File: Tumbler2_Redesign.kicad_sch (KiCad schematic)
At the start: 4 parts

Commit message: Sketch out component placement
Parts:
- H1, H2, H3, H4: footprint MountingHole:MountingHole_3mm_Pad -> MountingHole:MountingHole_3mm_Pad_Via
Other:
- sheet MCU ports: added INT1; removed INT
- sheet Peripherals ports: added INT1; removed INT

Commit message: Fix bus merging and add net classes
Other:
- sheet MCU ports: added {MOT_A}, {MOT_B}; removed {MOT1}, {MOT2}
- sheet Peripherals ports: added {MOT_A}, {MOT_B}; removed {MOT1}, {MOT2}
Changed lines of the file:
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@@
 	)
 	(bus_alias "USB1"
-		(members "DP" "DM")
+		(members "DP_1" "DN_1")
 	)
 	(bus_alias "USB2"
-		(members "DP" "DM")
+		(members "DP_2" "DN_2")
 	)
 	(circle
@@
 			)
 		)
-		(pin "{MOT1}" bidirectional
-			(at 198.12 102.87 0)
-			(effects
-				(font
-					(size 1.27 1.27)
-				)
-				(justify right)
-			)
-		)
-		(pin "{MOT2}" bidirectional
-			(at 198.12 106.68 0)
-			(effects
-				(font
-					(size 1.27 1.27)
-				)
-				(justify right)
-			)
-		)
 		(pin "RGB" output
 			(at 198.12 121.92 0)
@@
 		(pin "INT1" input
 			(at 198.12 90.17 0)
+			(effects
+				(font
+					(size 1.27 1.27)
+				)
+				(justify right)
+			)
+		)
+		(pin "{MOT_A}" bidirectional
+			(at 198.12 102.87 0)
+			(effects
+				(font
+					(size 1.27 1.27)
+				)
+				(justify right)
+			)
+		)
+		(pin "{MOT_B}" bidirectional
+			(at 198.12 106.68 0)
 			(effects
 				(font
@@
 			)
 		)
-		(pin "{MOT1}" input
-			(at 210.82 102.87 180)
-			(effects
-				(font
-					(size 1.27 1.27)
-				)
-				(justify left)
-			)
-		)
-		(pin "{MOT2}" input
-			(at 210.82 106.68 180)
-			(effects
-				(font
-					(size 1.27 1.27)
-				)
-				(justify left)
-			)
-		)
 		(pin "INT1" output
 			(at 210.82 90.17 180)
 			(effects
 				(font
+					(size 1.27 1.27)
+				)
+				(justify left)
+			)
+		)
+		(pin "{MOT_A}" input
+			(at 210.82 102.87 180)
+			(effects
+				(font
+					(size 1.27 1.27)
+				)
+				(justify left)
+			)
+		)
+		(pin "{MOT_B}" input
+			(at 210.82 106.68 180)
+			(effects
+				(font

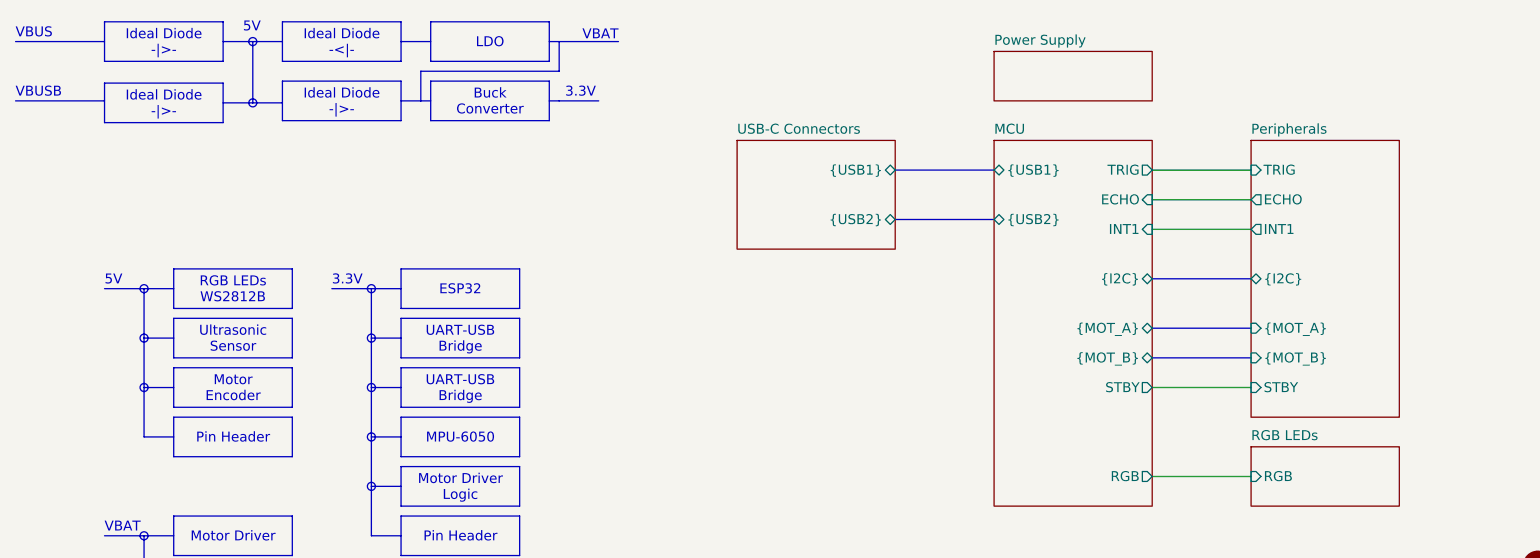
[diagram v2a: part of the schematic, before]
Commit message: Continue layout and update schematic
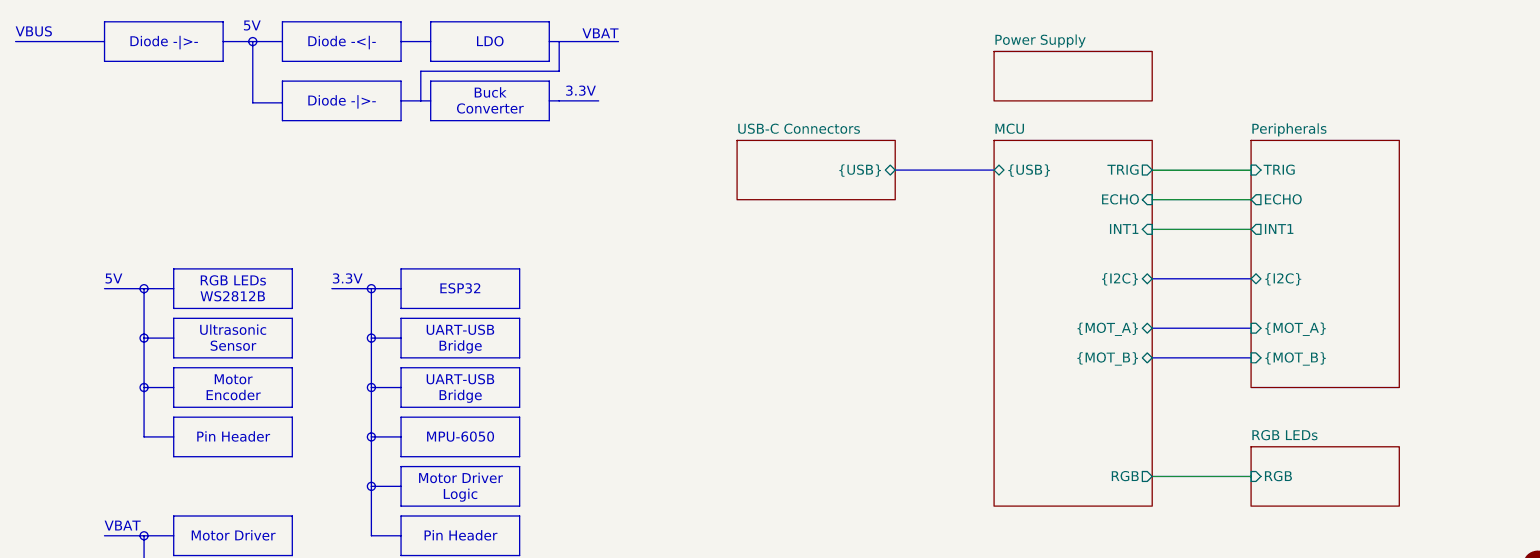
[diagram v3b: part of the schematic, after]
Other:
- sheet MCU ports: added {USB}; removed STBY, {USB1}, {USB2}
- sheet Peripherals ports: added none; removed STBY
- sheet USB-C Connectors ports: added {USB}; removed {USB1}, {USB2}
- note removed: "VBUSB"

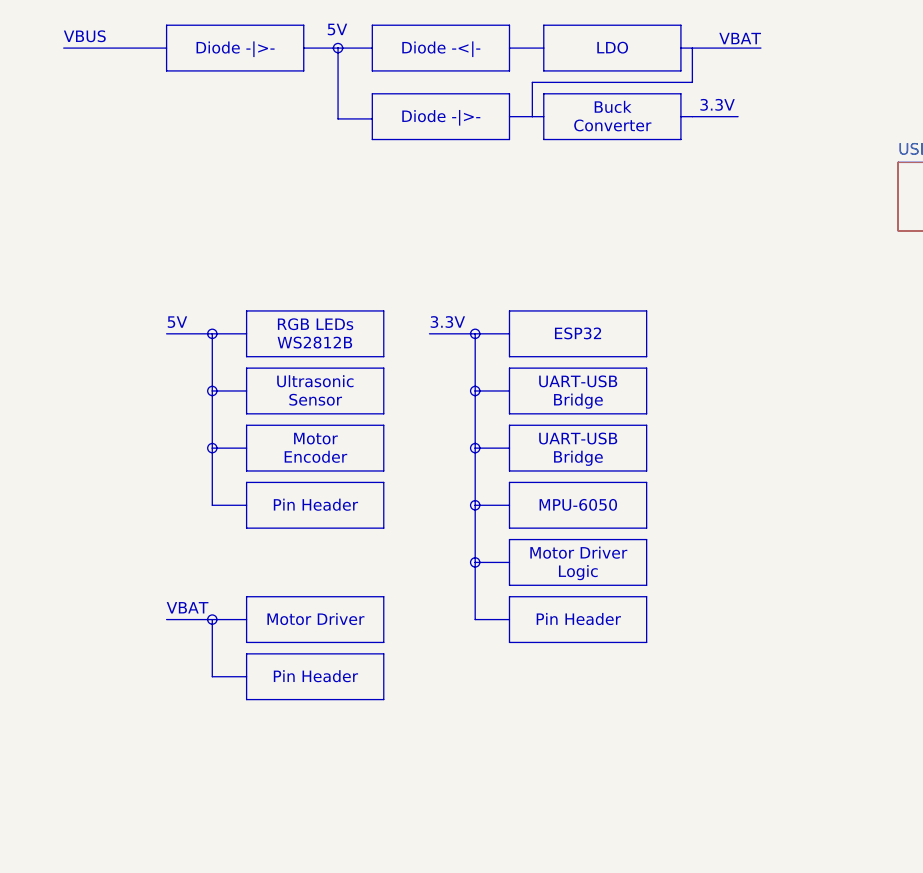
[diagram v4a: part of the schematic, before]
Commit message: Document strapping pins
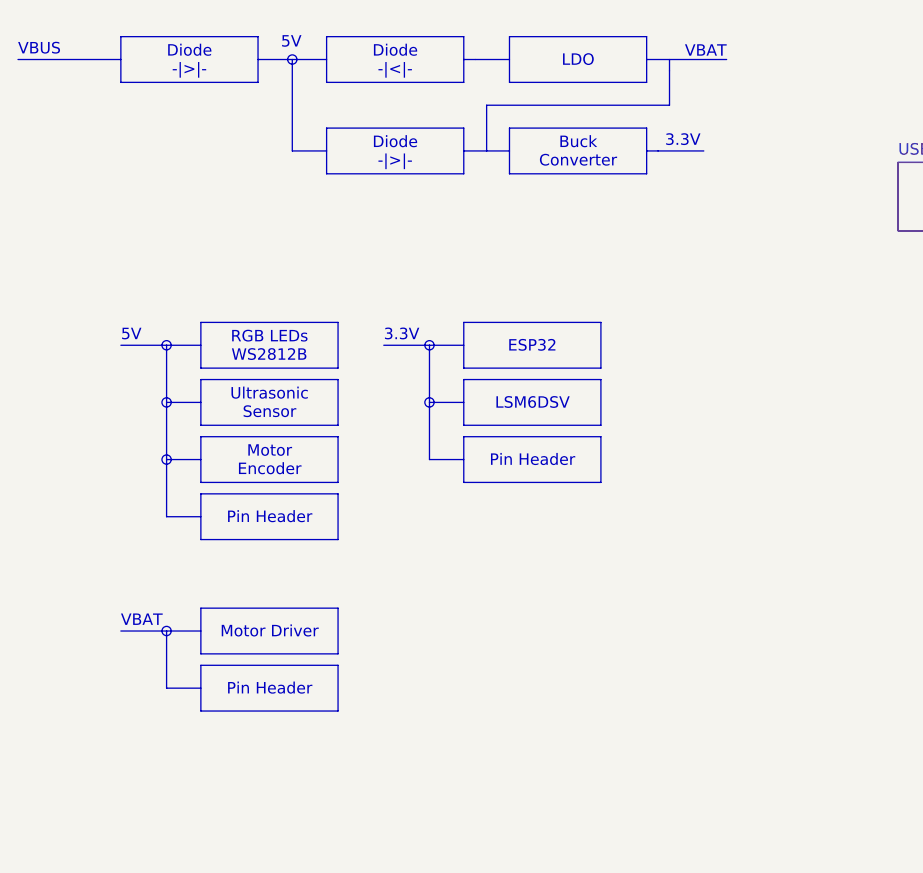
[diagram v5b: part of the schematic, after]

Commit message: Add todo list and update block diagram
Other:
- note added: "TODO: Verify output voltage levels for HC-SR04 (ECHO pin) and motor encoder Confirm whether logic HIGH is 5V, 3.3V, or lower (~2V possible) Check whether 5V or 3.3V HC-SR04 variant is used in current robots Measure actual PCB mounting hole positions Verify pin header pinout for line sensor PCB (B2B module)"
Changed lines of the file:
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@@
-	)
-	(circle
-		(center 63.5 130.81)
-		(radius 0.5142)
-		(stroke
-			(width 0)
-			(type solid)
-		)
-		(fill
-			(type color)
-			(color 0 0 194 1)
-		)
 	)
 	(circle
@@
 		)
 	)
+	(text "TODO:\nVerify output voltage levels for HC-SR04 (ECHO pin) and motor encoder\n	Confirm whether logic HIGH is 5V, 3.3V, or lower (~2V possible)\nCheck whether 5V or 3.3V HC-SR04 variant is used in current robots\nMeasure actual PCB mounting hole positions\nVerify pin header pinout for line sensor PCB (B2B module)"
+		(exclude_from_sim no)
+		(at 23.368 28.956 0)
+		(effects
+			(font
+				(size 1.27 1.27)
+			)
+			(justify left)
+		)
+	)
 	(text "VBUS"
 		(exclude_from_sim no)
@@
 	(text "VBAT"
 		(exclude_from_sim no)
-		(at 58.42 129.794 0)
+		(at 58.42 127.254 0)
 		(effects
 			(font
@@
 		)
 	)
-	(text_box "Pin Header\n"
-		(exclude_from_sim no)
-		(at 67.31 134.62 0)
-		(size 15.24 5.08)
-		(margins 0.9525 0.9525 0.9525 0.9525)
-		(stroke
-			(width 0)
-			(type solid)
-		)
-		(fill
-			(type none)
-		)
-		(effects
-			(font
-				(size 1.27 1.27)
-			)
-		)
-	)
 	(text_box "Motor Driver"
 		(exclude_from_sim no)
-		(at 67.31 128.27 0)
+		(at 67.31 125.73 0)
 		(size 15.24 5.08)
 		(margins 0.9525 0.9525 0.9525 0.9525)
@@
 	(polyline
 		(pts
-			(xy 63.5 137.16) (xy 67.31 137.16)
-		)
-		(stroke
-			(width 0)
-			(type default)
-		)
-	)
-	(polyline
-		(pts
 			(xy 63.5 105.41) (xy 67.31 105.41)
 		)
@@
 	(polyline
 		(pts
-			(xy 63.5 130.81) (xy 63.5 137.16)
-		)
-		(stroke
-			(width 0)
-			(type default)
-		)
-	)
-	(polyline
-		(pts
 			(xy 46.99 67.31) (xy 58.42 67.31)
 		)
@@
 	(polyline
 		(pts
-			(xy 58.42 130.81) (xy 67.31 130.81)
-		)
-		(stroke
+			(xy 58.42 128.27) (xy 67.31 128.27)
+		)
+		(stroke

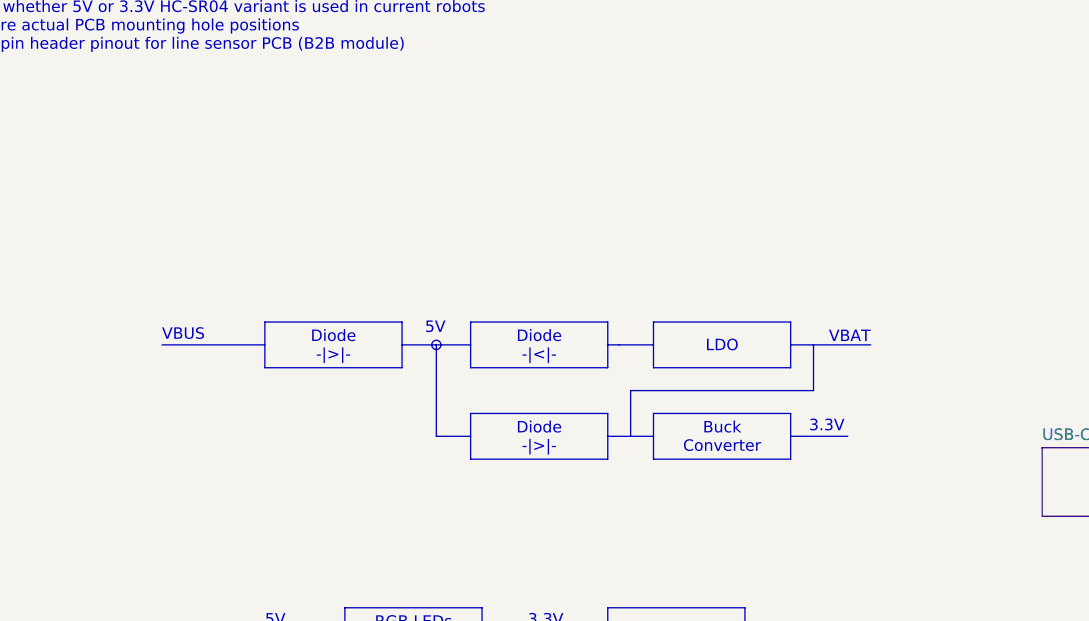
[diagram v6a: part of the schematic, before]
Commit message: cleanup schemati, replaced some caps from 0603 to 0805 around Linear Regulator
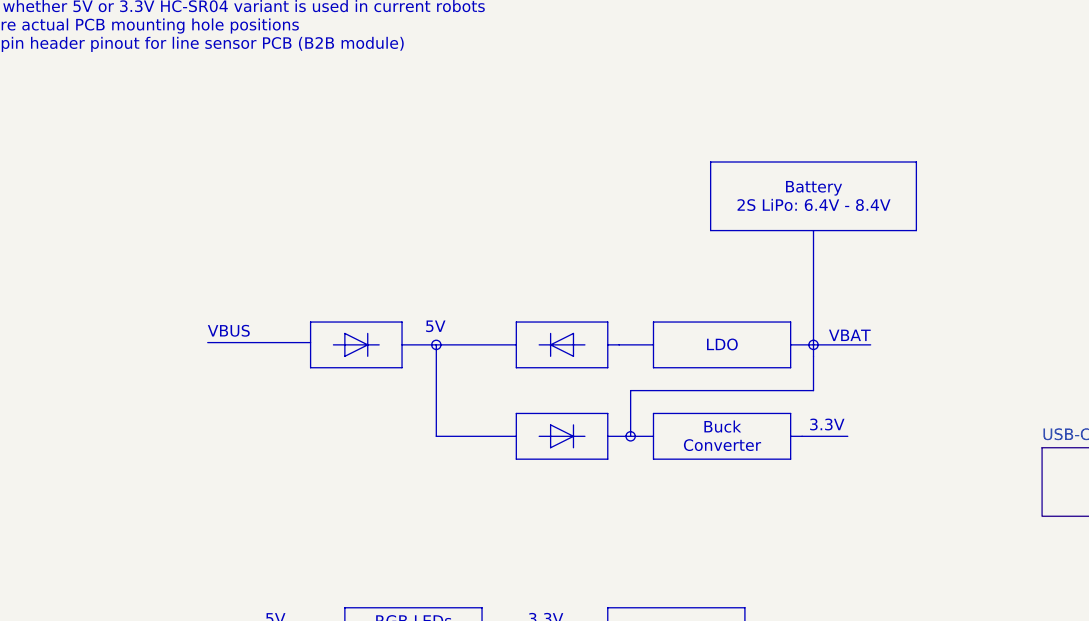
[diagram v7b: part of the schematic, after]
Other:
- company: (none) -> ${COMPANY}
- title: Tumbler 2 Redesign -> ${TITLE}
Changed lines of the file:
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@@
 	(paper "A4")
 	(title_block
-		(title "Tumbler 2 Redesign")
-		(rev "1.0")
+		(title "${TITLE}")
+		(date "2026-03-28")
+		(rev "${REVISION}")
+		(company "${COMPANY}")
+		(comment 1 "${AUTHOR1}, ${AUTHOR2}, ${AUTHOR3} ")
 	)
 	(bus_alias "UART"
@@
 	(bus_alias "USB"
 		(members "DP" "DN")
+	)
+	(circle
+		(center 99.06 77.47)
+		(radius 0.5142)
+		(stroke
+			(width 0)
+			(type solid)
+		)
+		(fill
+			(type color)
+			(color 0 0 194 1)
+		)
 	)
 	(circle
@@
 	)
 	(circle
+		(center 119.38 67.31)
+		(radius 0.5142)
+		(stroke
+			(width 0)
+			(type solid)
+		)
+		(fill
+			(type color)
+			(color 0 0 194 1)
+		)
+	)
+	(circle
 		(center 63.5 105.41)
 		(radius 0.5142)
@@
 	(text "VBUS"
 		(exclude_from_sim no)
-		(at 46.99 66.294 0)
+		(at 52.07 66.04 0)
 		(effects
 			(font
@@
 		)
 	)
-	(text_box "Diode\n-|>|-"
-		(exclude_from_sim no)
-		(at 81.28 74.93 0)
-		(size 15.24 5.08)
-		(margins 0.9525 0.9525 0.9525 0.9525)
-		(stroke
-			(width 0)
-			(type solid)
-		)
-		(fill
-			(type none)
-		)
-		(effects
-			(font
-				(size 1.27 1.27)
-			)
-		)
-	)
 	(text_box "Motor Encoder"
 		(exclude_from_sim no)
@@
 		)
 	)
+	(text_box ""
+		(exclude_from_sim no)
+		(at 96.52 74.93 0)
+		(size -10.16 5.08)
+		(margins 0.9525 0.9525 0.9525 0.9525)
+		(stroke
+			(width 0)
+			(type solid)
+		)
+		(fill
+			(type none)
+		)
+		(effects
+			(font
+				(size 1.27 1.27)
+			)
+		)
+	)
 	(text_box "Motor Driver"
 		(exclude_from_sim no)
@@
 		)
 	)
-	(text_box "Diode\n-|>|-"
-		(exclude_from_sim no)
-		(at 58.42 64.77 0)
-		(size 15.24 5.08)
+	(text_box "Battery\n2S LiPo: 6.4V - 8.4V"
+		(exclude_from_sim no)
+		(at 107.95 46.99 0)
+		(size 22.86 7.62)
+		(margins 0.9525 0.9525 0.9525 0.9525)
+		(stroke
+			(width 0)
+			(type solid)
+		)
+		(fill
+			(type none)
+		)
+		(effects
+			(font
+				(size 1.27 1.27)
+			)
+		)
+	)
+	(text_box ""
+		(exclude_from_sim no)
+		(at 73.66 64.77 0)
+		(size -10.16 5.08)
 		(margins 0.9525 0.9525 0.9525 0.9525)
 		(stroke
@@
 		)
 	)
-	(text_box "Diode\n-|<|-"
-		(exclude_from_sim no)
-		(at 81.28 64.77 0)
-		(size 15.24 5.08)
+	(text_box ""
+		(exclude_from_sim no)
+		(at 86.36 64.77 0)
+		(size 10.16 5.08)
 		(margins 0.9525 0.9525 0.9525 0.9525)
 		(stroke
@@
 	(polyline
 		(pts
+			(xy 69.85 67.31) (xy 67.31 66.04)
+		)
+		(stroke
+			(width 0)
+			(type default)
+		)
+	)
+	(polyline
+		(pts
 			(xy 119.38 67.31) (xy 119.38 68.58)
 		)
@@
 	(polyline
 		(pts
+			(xy 69.85 68.58) (xy 69.85 66.04)
+		)
+		(stroke
+			(width 0)
+			(type default)
+		)
+	)
+	(polyline
+		(pts
 			(xy 92.71 105.41) (xy 92.71 111.76)
 		)
@@
 	(polyline
 		(pts
+			(xy 88.9 77.47) (xy 93.98 77.47)
+		)
+		(stroke
+			(width 0)
+			(type default)
+		)
+	)
+	(polyline
+		(pts
 			(xy 125.73 67.31) (xy 116.84 67.31)
 		)
@@
 		)
 	)
+	(polyline
+		(pts
+			(xy 92.71 77.47) (xy 90.17 76.2)
+		)
+		(stroke
+			(width 0)
+			(type default)
+		)
+	)
+	(polyline
+		(pts
+			(xy 119.38 67.31) (xy 119.38 54.61)
+		)
+		(stroke
+			(width 0)
+			(type default)
+		)
+	)
+	(polyline
+		(pts
+			(xy 92.71 78.74) (xy 92.71 76.2)
+		)
+		(stroke
+			(width 0)
+			(type default)
+		)
+	)
 	(bus
 		(pts
@@
 	(polyline
 		(pts
+			(xy 66.04 67.31) (xy 71.12 67.31)
+		)
+		(stroke
+			(width 0)
+			(type default)
+		)
+	)
+	(polyline
+		(pts
+			(xy 90.17 76.2) (xy 90.17 78.74)
+		)
+		(stroke
+			(width 0)
+			(type default)
+		)
+	)
+	(polyline
+		(pts
 			(xy 119.38 72.39) (xy 119.38 68.58)
 		)
@@
 	(polyline
 		(pts
-			(xy 77.47 67.31) (xy 81.28 67.31)
+			(xy 77.47 67.31) (xy 86.36 67.31)
+		)
+		(stroke
+			(width 0)
+			(type default)
+		)
+	)
+	(polyline
+		(pts
+			(xy 90.17 68.58) (xy 90.17 66.04)
 		)
 		(stroke
@@
 	(polyline
 		(pts
+			(xy 93.98 67.31) (xy 88.9 67.31)
+		)
+		(stroke
+			(width 0)
+			(type default)
+		)
+	)
+	(polyline
+		(pts
 			(xy 99.06 77.47) (xy 96.52 77.47)
 		)
@@
 	(polyline
 		(pts
+			(xy 67.31 66.04) (xy 67.31 68.58)
+		)
+		(stroke
+			(width 0)
+			(type default)
+		)
+	)
+	(polyline
+		(pts
 			(xy 77.47 77.47) (xy 77.47 67.31)
 		)
@@
 	(polyline
 		(pts
-			(xy 46.99 67.31) (xy 58.42 67.31)
+			(xy 90.17 67.31) (xy 92.71 66.04)
+		)
+		(stroke
+			(width 0)
+			(type default)
+		)
+	)
+	(polyline
+		(pts
+			(xy 69.85 67.31) (xy 67.31 68.58)
+		)
+		(stroke
+			(width 0)
+			(type default)
+		)
+	)
+	(polyline
+		(pts
+			(xy 52.07 67.056) (xy 63.5 67.056)
 		)
 		(stroke
@@
 	(polyline
 		(pts
-			(xy 77.47 77.47) (xy 81.28 77.47)
+			(xy 92.71 77.47) (xy 90.17 78.74)
+		)
+		(stroke
+			(width 0)
+			(type default)
+		)
+	)
+	(polyline
+		(pts
+			(xy 77.47 77.47) (xy 86.36 77.47)
 		)
 		(stroke
@@
 		)
 	)
+	(polyline
+		(pts
+			(xy 92.71 66.04) (xy 92.71 68.58)
+		)
+		(stroke
+			(width 0)
+			(type default)
+		)
+	)
 	(wire
 		(pts
@@
 		)
 		(stroke
+			(width 0)
+			(type default)
+		)
+	)
+	(polyline
+		(pts
+			(xy 90.17 67.31) (xy 92.71 68.58)
+		)
+		(stroke
